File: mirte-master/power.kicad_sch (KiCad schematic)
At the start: 2 parts, among them J25 USB_A, Q1 DMG2305UX

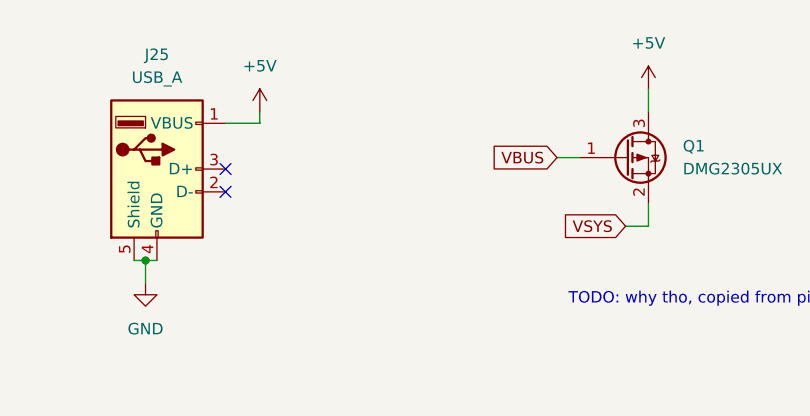
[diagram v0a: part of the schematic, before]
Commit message: add kerco/elcos
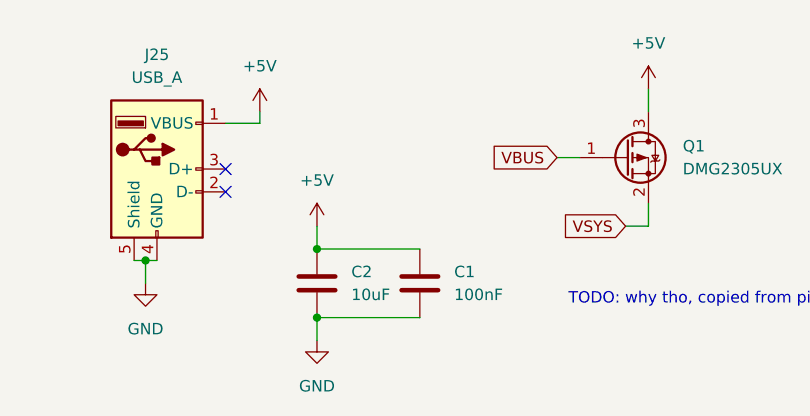
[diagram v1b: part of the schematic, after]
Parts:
- added C1: 100nF, Capacitor_SMD:C_0805_2012Metric, symbol Device:C
- added C2: 10uF, Capacitor_SMD:C_0805_2012Metric, symbol Device:C
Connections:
- net +5V: now also C1.1, C2.1
- net GND: now also C1.2, C2.2
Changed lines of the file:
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@@
 (kicad_sch (version 20230121) (generator eeschema)
   (paper "A4")
+  (junction (at 160.02 152.4) (diameter 0) (color 0 0 0 0)
+  )
+  (junction (at 160.02 160.02) (diameter 0) (color 0 0 0 0)
+  )
   (junction (at 140.97 153.67) (diameter 0) (color 0 0 0 0)
   )
   (no_connect (at 149.86 143.51))
   (no_connect (at 149.86 146.05))
+  (wire (pts (xy 160.02 160.02) (xy 160.02 162.56))
+    (stroke (width 0) (type default))
+  )
+  (wire (pts (xy 160.02 149.86) (xy 160.02 152.4))
+    (stroke (width 0) (type default))
+  )
   (wire (pts (xy 153.67 137.16) (xy 153.67 138.43))
     (stroke (width 0) (type default))
@@
     (stroke (width 0) (type default))
   )
+  (wire (pts (xy 171.45 160.02) (xy 160.02 160.02))
+    (stroke (width 0) (type default))
+  )
   (wire (pts (xy 153.67 138.43) (xy 149.86 138.43))
     (stroke (width 0) (type default))
@@
   )
   (wire (pts (xy 96.52 50.8) (xy 104.14 50.8))
+    (stroke (width 0) (type default))
+  )
+  (wire (pts (xy 171.45 152.4) (xy 160.02 152.4))
     (stroke (width 0) (type default))
   )
@@
     (effects (font (size 1.27 1.27)) (justify right))
   )
+  (symbol (lib_id "power:+5V") (at 160.02 149.86 0) (unit 1)
+    (in_bom yes) (on_board yes) (dnp no) (fields_autoplaced)
+    (property "Reference" "#PWR011" (at 160.02 153.67 0)
+      (effects (font (size 1.27 1.27)) hide)
+    )
+    (property "Value" "+5V" (at 160.02 144.78 0)
+      (effects (font (size 1.27 1.27)))
+    )
+    (property "Footprint" "" (at 160.02 149.86 0)
+      (effects (font (size 1.27 1.27)) hide)
+    )
+    (property "Datasheet" "" (at 160.02 149.86 0)
+      (effects (font (size 1.27 1.27)) hide)
+    )
+    (pin "1")
+    (instances
+      (project "mirte-master"
+        (path "/19794465-0368-488c-958e-83b02754ebd6/17ebe4c8-09bb-4699-976c-396d27e4a3f5"
+          (reference "#PWR011") (unit 1)
+        )
+      )
+    )
+  )
   (symbol (lib_id "power:+5V") (at 196.85 134.62 0) (unit 1)
     (in_bom yes) (on_board yes) (dnp no) (fields_autoplaced)
@@
     )
   )
+  (symbol (lib_id "Device:C") (at 160.02 156.21 0) (unit 1)
+    (in_bom yes) (on_board yes) (dnp no) (fields_autoplaced)
+    (property "Reference" "C2" (at 163.83 154.94 0)
+      (effects (font (size 1.27 1.27)) (justify left))
+    )
+    (property "Value" "10uF" (at 163.83 157.48 0)
+      (effects (font (size 1.27 1.27)) (justify left))
+    )
+    (property "Footprint" "Capacitor_SMD:C_0805_2012Metric" (at 160.9852 160.02 0)
+      (effects (font (size 1.27 1.27)) hide)
+    )
+    (property "Datasheet" "~" (at 160.02 156.21 0)
+      (effects (font (size 1.27 1.27)) hide)
+    )
+    (pin "2")
+    (pin "1")
+    (instances
+      (project "mirte-master"
+        (path "/19794465-0368-488c-958e-83b02754ebd6/17ebe4c8-09bb-4699-976c-396d27e4a3f5"
+          (reference "C2") (unit 1)
+        )
+      )
+    )
+  )
   (symbol (lib_id "power:+5V") (at 153.67 137.16 0) (unit 1)
     (in_bom yes) (on_board yes) (dnp no) (fields_autoplaced)
@@
         (path "/19794465-0368-488c-958e-83b02754ebd6/17ebe4c8-09bb-4699-976c-396d27e4a3f5"
           (reference "#PWR057") (unit 1)
+        )
+      )
+    )
+  )
+  (symbol (lib_id "Device:C") (at 171.45 156.21 0) (unit 1)
+    (in_bom yes) (on_board yes) (dnp no) (fields_autoplaced)
+    (property "Reference" "C1" (at 175.26 154.94 0)
+      (effects (font (size 1.27 1.27)) (justify left))
+    )
+    (property "Value" "100nF" (at 175.26 157.48 0)
+      (effects (font (size 1.27 1.27)) (justify left))
+    )
+    (property "Footprint" "Capacitor_SMD:C_0805_2012Metric" (at 172.4152 160.02 0)
+      (effects (font (size 1.27 1.27)) hide)
+    )
+    (property "Datasheet" "~" (at 171.45 156.21 0)
+      (effects (font (size 1.27 1.27)) hide)
+    )
+    (pin "2")
+    (pin "1")
+    (instances
+      (project "mirte-master"
+        (path "/19794465-0368-488c-958e-83b02754ebd6/17ebe4c8-09bb-4699-976c-396d27e4a3f5"
+          (reference "C1") (unit 1)
         )
       )
@@
         )
       )
+    )
+  )
+  (symbol (lib_id "power:GND") (at 160.02 162.56 0) (unit 1)
+    (in_bom yes) (on_board yes) (dnp no) (fields_autoplaced)
+    (property "Reference" "#PWR012" (at 160.02 168.91 0)
+      (effects (font (size 1.27 1.27)) hide)
+    )
+    (property "Value" "GND" (at 160.02 167.64 0)
+      (effects (font (size 1.27 1.27)))
+    )
+    (property "Footprint" "" (at 160.02 162.56 0)
+      (effects (font (size 1.27 1.27)) hide)
+    )
+    (property "Datasheet" "" (at 160.02 162.56 0)
+      (effects (font (size 1.27 1.27)) hide)
+    )
+    (pin "1")
+    (instances
+      (project "mirte-master"
+        (path "/19794465-0368-488c-958e-83b02754ebd6/17ebe4c8-09bb-4699-976c-396d27e4a3f5"
+          (reference "#PWR012") (unit 1)
+        )
+      )

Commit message: mirte master parts jclpcb fixed
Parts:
- C1: LCSC (none) -> C49678
- C2: LCSC (none) -> C15850
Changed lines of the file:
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@@
+      (effects (font (size 1.27 1.27)) hide)
+    )
+    (property "LCSC" "C15850" (at 160.02 156.21 0)
       (effects (font (size 1.27 1.27)) hide)
     )
@@
       (effects (font (size 1.27 1.27)) hide)
     )
+    (property "LCSC" "C49678" (at 171.45 156.21 0)
+      (effects (font (size 1.27 1.27)) hide)
+    )

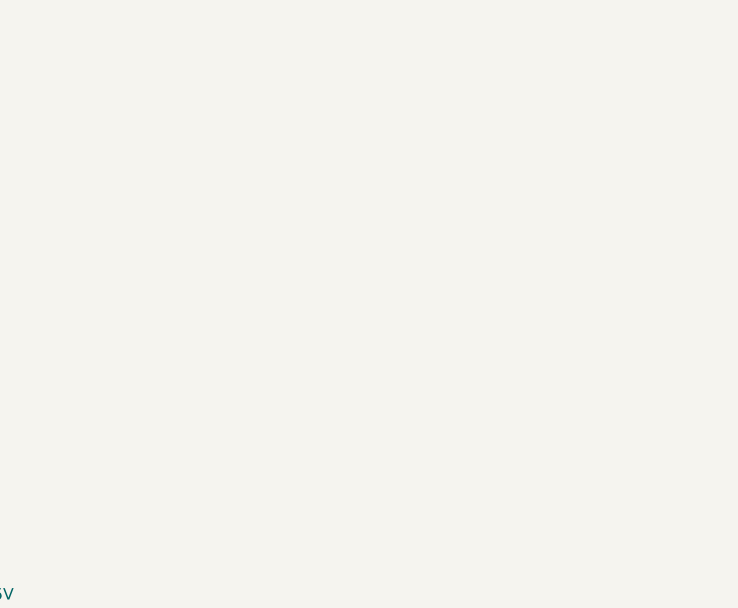
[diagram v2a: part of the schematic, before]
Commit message: add usb switcher + finalize mirte-master
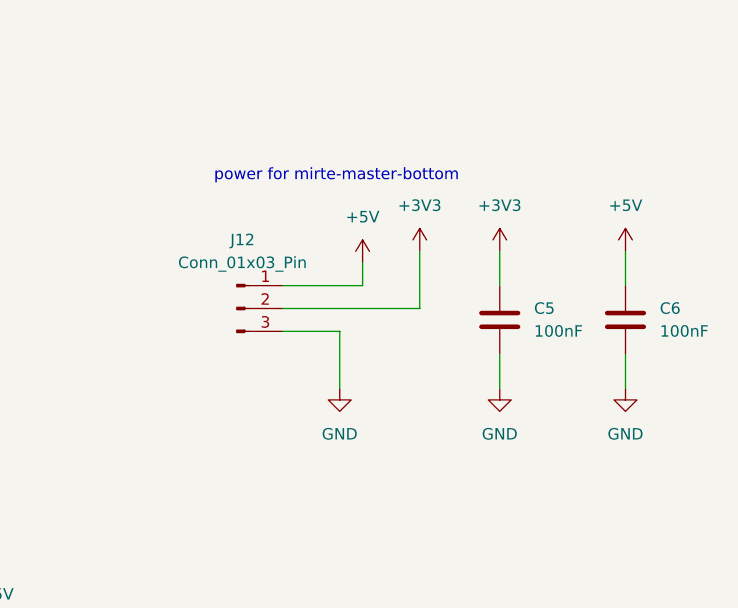
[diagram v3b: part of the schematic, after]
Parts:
- added C5, C6: 100nF, Capacitor_SMD:C_0805_2012Metric, symbol Device:C
- added J12: Conn_01x03_Pin, Connector_JST:JST_XH_B3B-XH-A_1x03_P2.50mm_Vertical, symbol Connector:Conn_01x03_Pin
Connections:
- net +5V: now also C6.1, J12.1 (Pin_1)
- net GND: now also C5.2, C6.2, J12.3 (Pin_3)
- new net +3V3: C5.1, J12.2 (Pin_2)
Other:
- note added: "power for mirte-master-bottom"

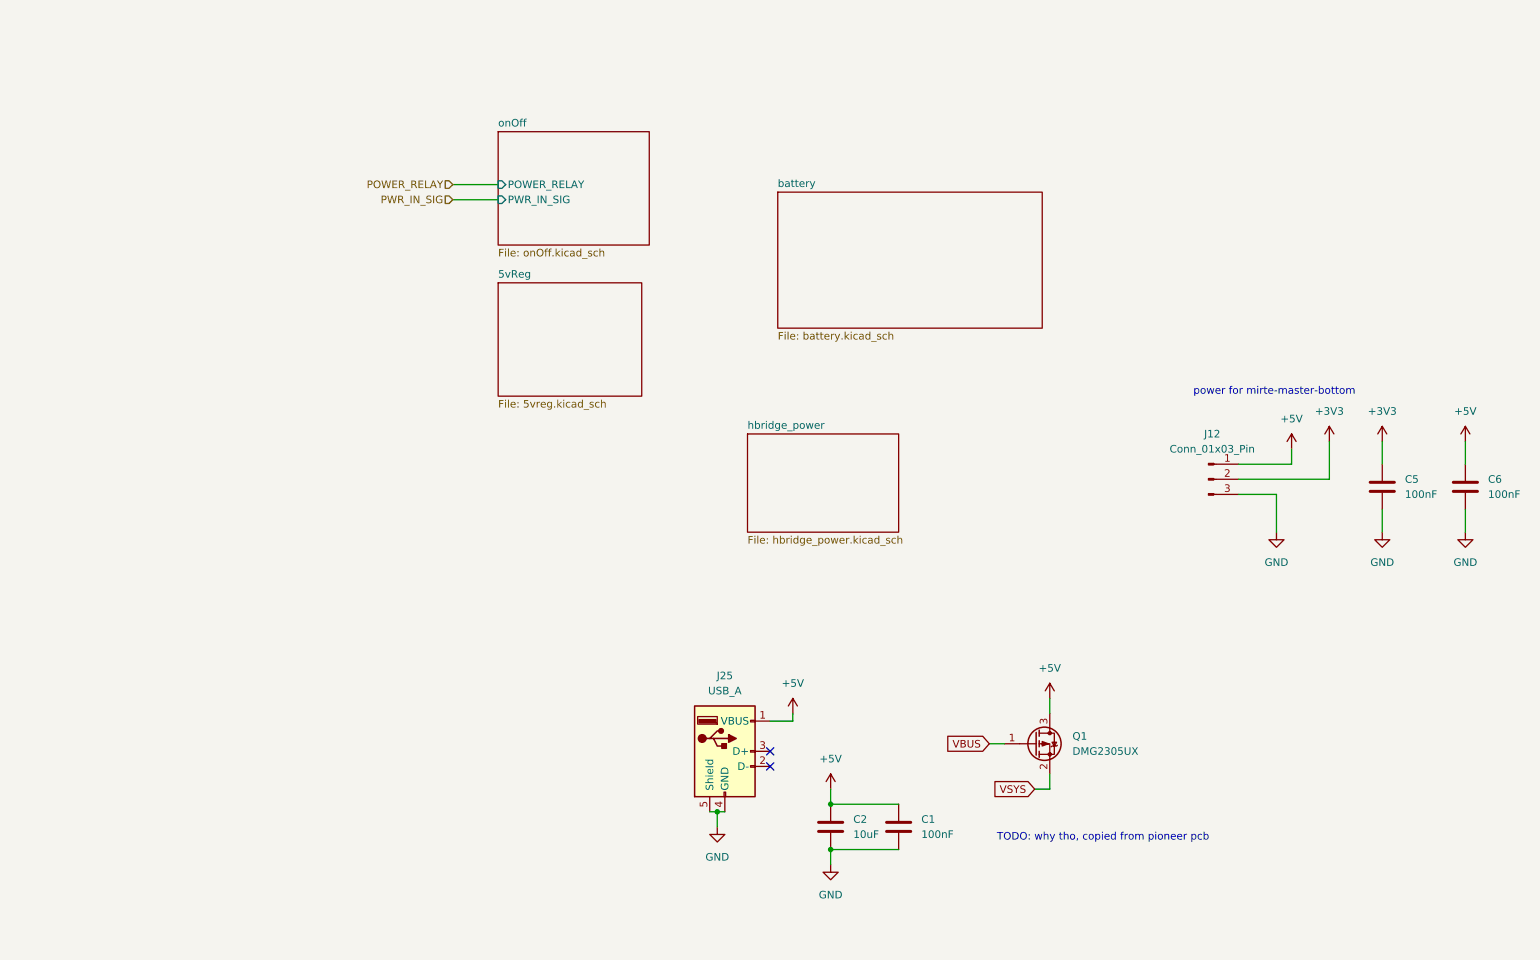
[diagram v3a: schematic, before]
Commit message: mirte-master schematic cleanup and readabilityimprovements
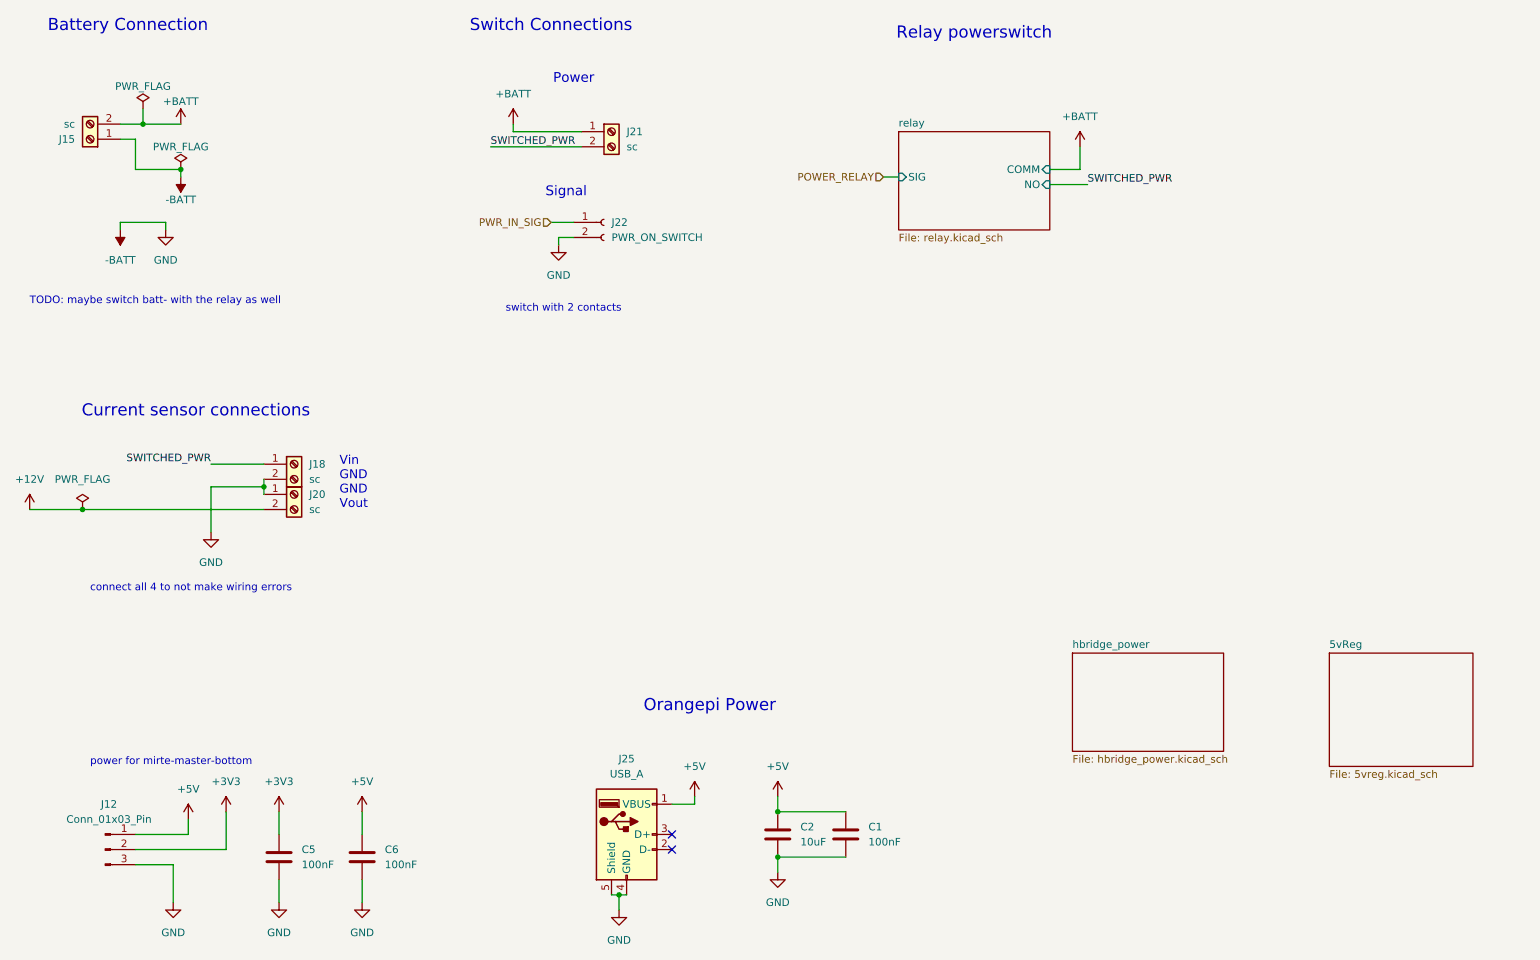
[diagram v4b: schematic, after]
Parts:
- removed Q1: DMG2305UX, Package_TO_SOT_SMD:SOT-23, symbol Transistor_FET:DMG2301L
- added J15, J18, J20, J21: sc, easyeda:CONN-TH_XY126V-5.0-2P, symbol Connector:Screw_Terminal_01x02
- added J22: PWR_ON_SWITCH, Connector_JST:JST_XH_B2B-XH-A_1x02_P2.50mm_Vertical, symbol Connector:Conn_01x02_Socket
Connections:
- net PWR_IN_SIG: now also J22.1 (Pin_1)
- net GND renamed -BATT
- net -BATT: now also J15.1 (Pin_1), J18.2 (Pin_2), J20.1 (Pin_1), J22.2 (Pin_2)
- new net +12V: J20.2 (Pin_2)
- new net +BATT: J15.2 (Pin_2), J21.1 (Pin_1)
- new net SWITCHED_PWR: J18.1 (Pin_1), J21.2 (Pin_2)
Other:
- removed sheet battery
- removed sheet onOff
- added sheet relay (relay.kicad_sch)
- note added: "Battery Connection"
- note added: "Current sensor connections"
- note added: "Orangepi Power"
- note added: "Power"
- note added: "Relay powerswitch"
- note added: "Signal"
- note added: "Switch Connections"
- note added: "TODO: maybe switch batt- with the relay as well"
- note added: "Vin GND GND Vout"
- note added: "connect all 4 to not make wiring errors"
- note added: "switch with 2 contacts"
- note removed: "TODO: why tho, copied from pioneer pcb"
- title: (none) -> ${PROJECTNAME}
- moved on the sheet: C1, C2, C5, C6, J12, J25
